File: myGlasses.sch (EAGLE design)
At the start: 16 parts

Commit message: Lunettes petit format corrige
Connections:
- net 3.3V: now also TRI_LED.A
- net GND: no longer TRI_LED.A
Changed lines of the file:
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@@
 <part name="TRI_LED" library="SparkFun-LED" deviceset="LED-TRICOLOR" device=""/>
 <part name="INTER" library="SparkFun-Electromechanical" deviceset="SWITCH-SPDT" device="PTH_LOCK"/>
-<part name="GND4" library="SparkFun-Aesthetics" deviceset="GND" device=""/>
 <part name="R1" library="microbuilder" deviceset="RESISTOR" device="1206" value="220"/>
 <part name="R2" library="microbuilder" deviceset="RESISTOR" device="1206" value="220"/>
@@
 <part name="GND9" library="SparkFun-Aesthetics" deviceset="GND" device=""/>
 <part name="SWD" library="SparkFun-Connectors" deviceset="M02" device="PTH"/>
+<part name="SUPPLY3" library="SparkFun-Aesthetics" deviceset="3.3V" device=""/>
 </parts>
 <sheets>
@@
 <instance part="TRI_LED" gate="G$1" x="129.54" y="43.18"/>
 <instance part="INTER" gate="1" x="15.24" y="134.62"/>
-<instance part="GND4" gate="1" x="149.86" y="40.64" rot="R90"/>
 <instance part="R1" gate="G$1" x="109.22" y="43.18"/>
 <instance part="R2" gate="G$1" x="109.22" y="38.1"/>
@@
 <instance part="GND9" gate="1" x="-119.38" y="76.2" rot="R180"/>
 <instance part="SWD" gate="G$1" x="35.56" y="0" rot="R90"/>
+<instance part="SUPPLY3" gate="G$1" x="149.86" y="40.64" rot="R270"/>
 </instances>
 <busses>
@@
 </segment>
 <segment>
-<pinref part="TRI_LED" gate="G$1" pin="A"/>
-<pinref part="GND4" gate="1" pin="GND"/>
-<wire x1="142.24" y1="40.64" x2="147.32" y2="40.64" width="0.1524" layer="91"/>
-</segment>
-<segment>
 <pinref part="C2" gate="G$1" pin="P$2"/>
 <pinref part="GND6" gate="1" pin="GND"/>
@@
 <pinref part="SUPPLY2" gate="G$1" pin="3.3V"/>
 <wire x1="27.94" y1="66.04" x2="27.94" y2="73.66" width="0.1524" layer="91"/>
+</segment>
+<segment>
+<pinref part="TRI_LED" gate="G$1" pin="A"/>
+<pinref part="SUPPLY3" gate="G$1" pin="3.3V"/>
+<wire x1="142.24" y1="40.64" x2="149.86" y2="40.64" width="0.1524" layer="91"/>
 </segment>
 </net>
@@
 <wire x1="-35.56" y1="68.58" x2="-45.72" y2="68.58" width="0.1524" layer="91"/>
 <junction x="10.16" y="134.62"/>
+<junction x="-45.72" y="68.58"/>
 </segment>
 </net>
@@
 <wire x1="-109.22" y1="40.64" x2="-109.22" y2="68.58" width="0.1524" layer="91"/>
 <junction x="-109.22" y="68.58"/>
+<junction x="-96.52" y="68.58"/>
 </segment>
 </net>
@@
 </sheet>
 </sheets>
+<errors>
+</errors>
 </schematic>
 </drawing>

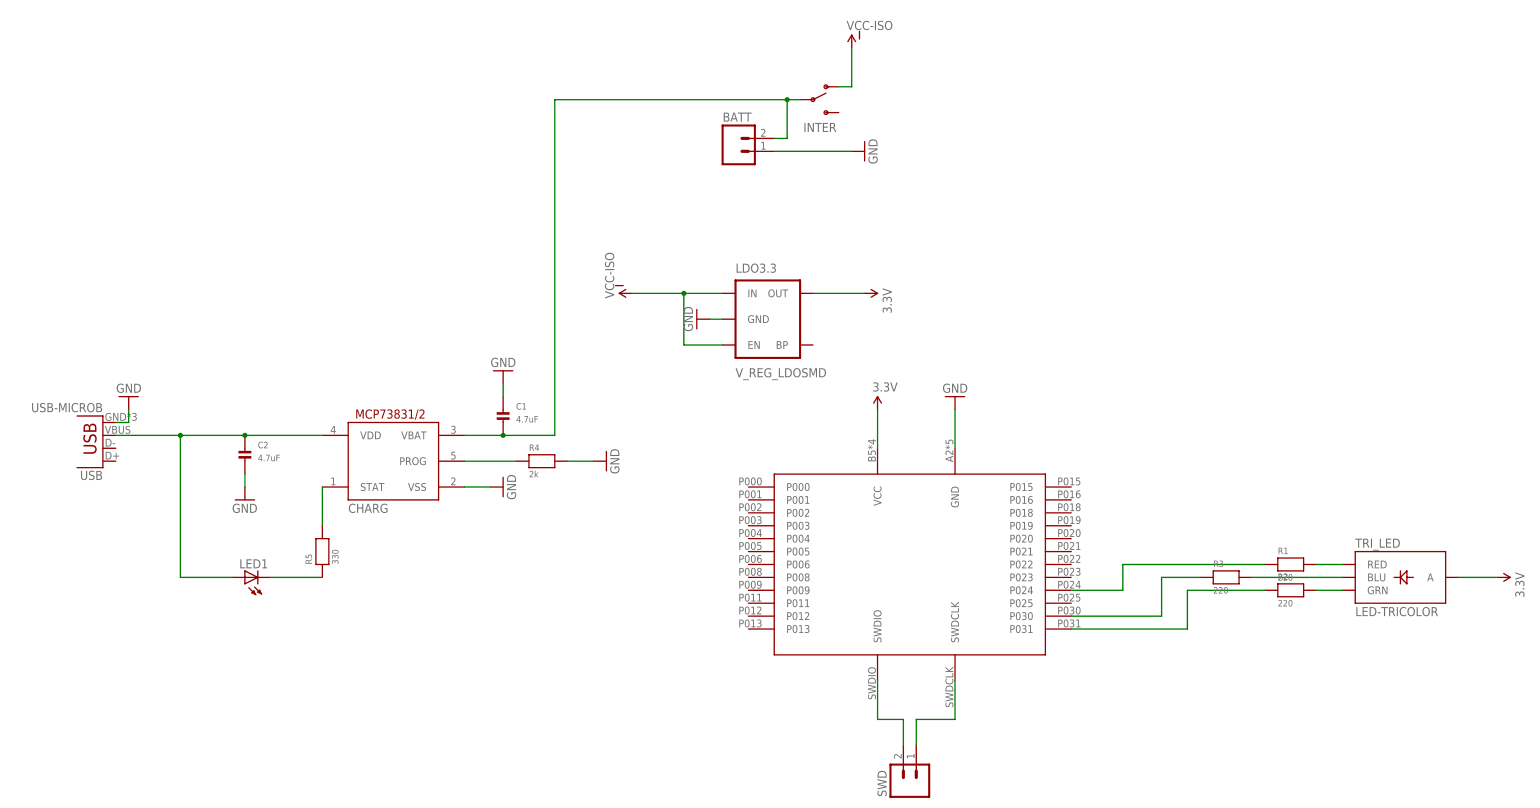
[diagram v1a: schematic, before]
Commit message: Put a ML1220 cell First routing
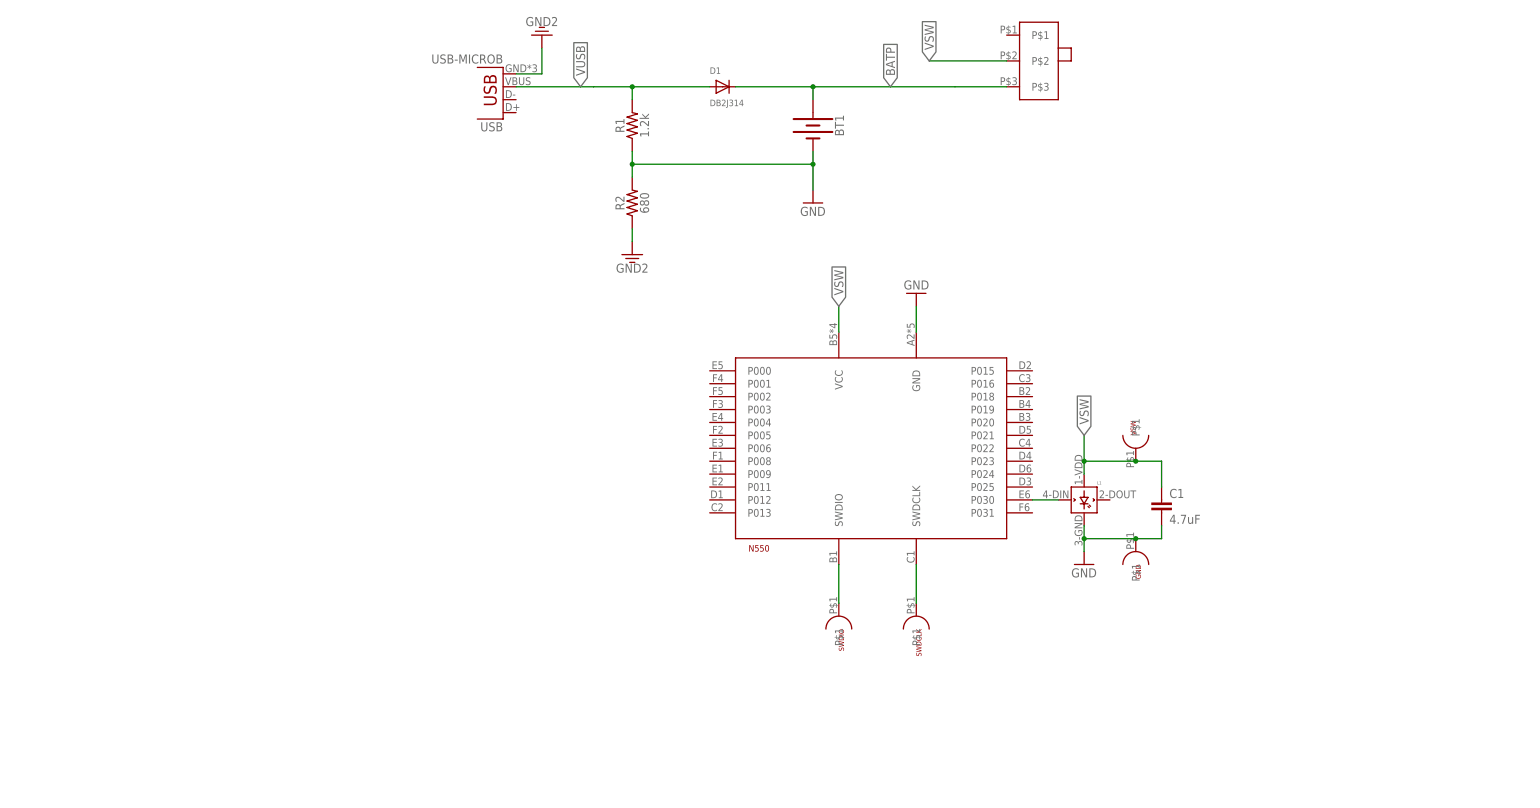
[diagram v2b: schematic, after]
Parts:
- removed BATT: (no value), SparkFun-Connectors:M02PTH3
- removed C2: 4.7uF, microbuilder:CAP_CERAMIC1206
- removed CHARG: MCP73831/OT, adafruit:MCP73831/OT
- removed INTER: (no value), SparkFun-Electromechanical:SWITCH-SPDTPTH_LOCK
- removed LDO3.3: V_REG_LDOSMD, SparkFun-PowerIC:V_REG_LDOSMD
- removed LED1: (no value), adafruit:LEDCHIPLED_1206
- removed R3: 220, microbuilder:RESISTOR1206
- removed R4: 2k, microbuilder:RESISTOR1206
- removed R5: 330, microbuilder:RESISTOR1206
- removed SWD: (no value), SparkFun-Connectors:M02PTH
- removed TRI_LED: LED-TRICOLOR, SparkFun-LED:LED-TRICOLOR
- added BT1: (no value), SparkFun-Batteries:BATTERY-12MM_PTH
- added D1: DB2J314, adafruit:DIODESOD-323F
- added GND, SWDCLK, SWDIO, VSW: TESTPOINT, test_points:TESTPOINT
- added L1: WS2812B, adafruit:WS2812B
- added U$1: JS102011SAQN, JS102011SAQN:JS102011SAQN
- C1: device microbuilder:CAP_CERAMIC1206 -> SparkFun-Capacitors:0.1UF-0603-25V-5%
- N550: value N548 -> N5150; device N548:N548 -> N5:N5150
- R1: value 220 -> 1.2k; device microbuilder:RESISTOR1206 -> SparkFun-Resistors:4.7KOHM-0603-1/10W-1%
- R2: value 220 -> 680; device microbuilder:RESISTOR1206 -> SparkFun-Resistors:4.7KOHM-0603-1/10W-1%
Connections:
- removed net N$10: N550.SWDCLK, SWD.1
- removed net N$11: N550.P024, R1.1
- removed net N$12: N550.P030, R3.1
- removed net N$13: N550.P031, R2.1
- removed net N$2: R1.2, TRI_LED.RED
- removed net N$4: R3.2, TRI_LED.BLU
- removed net N$5: C2.P$1, CHARG.VDD, LED1.A, USB.VBUS
- removed net N$6: N550.SWDIO, SWD.2
- removed net N$7: CHARG.PROG, R4.1
- removed net N$8: CHARG.STAT, R5.2
- removed net N$9: LED1.C, R5.1
- removed net VCC-ISO: INTER.O, LDO3.3.EN, LDO3.3.IN
- new net BATP: BT1.+, D1.C, U$1.P$3
- new net NEO: L1.DIN, N550.P030
- new net VSW: C1.1, L1.VDD, N550.VCC, U$1.P$2, VSW.P$1
- new net VUSB: D1.A, R1.2, USB.VBUS
- net 3.3V: now also R2.1, USB.GND; no longer LDO3.3.OUT, N550.VCC, TRI_LED.A
- net GND: now also BT1.-, C1.2, GND.P$1, L1.GND, R1.1, R2.2; no longer BATT.1, C1.P$1, C2.P$2, CHARG.VSS, LDO3.3.GND, R4.2, USB.GND
- net N$1: now also N550.SWDIO, SWDIO.P$1; no longer BATT.2, C1.P$2, CHARG.VBAT, INTER.P
- net N$3: now also N550.SWDCLK, SWDCLK.P$1; no longer R2.2, TRI_LED.GRN
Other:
- moved on the sheet: C1, USB
